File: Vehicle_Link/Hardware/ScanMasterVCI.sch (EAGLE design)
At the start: 97 parts, among them IC1 XMEGA32A4U, IC2 TL331, Q1 MMBT4403, Q10 ZXMP6A17G, Q2 MMBT3904, Q3 MMBT3904, Q4 MMBT4403, Q7 MMBT3904, Q8 MMBT4403, Q9 MMPQ3904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

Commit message: CCD RX circuit tested. Don't have the firmware in a state to test the TX but I want to move forward with new boards for testing. I've finished re-laying out the board. Made a minor change to J1850, switched to a comparator for the RX.
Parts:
- added IC3: TL331, linear:TL331
- added R41: 10k, adafruit:R-US_R0603
- R2: value 7.5k -> 1k
- R3: value 5k -> 1k
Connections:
- removed net SCI-A-ENGINE-EN: IC1.PB0
- removed net SCI-A-TRANS-EN: IC1.PB2
- removed net SCI-B-ENGINE-EN: IC1.PB1
- removed net SCI-B-TRANS-EN: IC1.PB3
- new net N$37: IC3.+IN, R2.1, R3.2
- net +3V3: now also IC3.V+, R41.2
- net +8V: now also R2.2
- net CCD-RX: now also R41.1
- net GND: now also IC3.GND
- net J1850VPW-RX: now also IC3.OUT; no longer R2.1, R3.2
- net J1962-2: now also IC3.-IN; no longer R2.2
- net SCI-A-EN: now also IC1.PB0
- net SCI-B-EN: now also IC1.PB1
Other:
- moved on the sheet: R2, R3

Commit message: Worked on the board layout some more - tried to trim down on some vias.
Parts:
- removed C3: 0.1uF, adafruit:C-USC0603
- removed R41: 10k, adafruit:R-US_R0603
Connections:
- net +3V3: no longer C3.1, R41.2
- net CCD-RX: no longer R41.1
- net GND: no longer C3.2
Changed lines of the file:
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@@
 <grid distance="0.1" unitdist="inch" unit="inch" style="lines" multiple="1" display="no" altdistance="0.01" altunitdist="inch" altunit="inch"/>
 <layers>
-<layer number="1" name="Top" color="4" fill="1" visible="yes" active="no"/>
-<layer number="16" name="Bottom" color="1" fill="1" visible="yes" active="no"/>
-<layer number="17" name="Pads" color="2" fill="1" visible="yes" active="no"/>
-<layer number="18" name="Vias" color="2" fill="1" visible="yes" active="no"/>
-<layer number="19" name="Unrouted" color="6" fill="1" visible="yes" active="no"/>
-<layer number="20" name="Dimension" color="24" fill="1" visible="yes" active="no"/>
-<layer number="21" name="tPlace" color="7" fill="1" visible="yes" active="no"/>
-<layer number="22" name="bPlace" color="7" fill="1" visible="yes" active="no"/>
-<layer number="23" name="tOrigins" color="15" fill="1" visible="yes" active="no"/>
-<layer number="24" name="bOrigins" color="15" fill="1" visible="yes" active="no"/>
-<layer number="25" name="tNames" color="7" fill="1" visible="yes" active="no"/>
-<layer number="26" name="bNames" color="7" fill="1" visible="yes" active="no"/>
-<layer number="27" name="tValues" color="7" fill="1" visible="yes" active="no"/>
-<layer number="28" name="bValues" color="7" fill="1" visible="yes" active="no"/>
+<layer number="1" name="Top" color="4" fill="1" visible="no" active="no"/>
+<layer number="16" name="Bottom" color="1" fill="1" visible="no" active="no"/>
+<layer number="17" name="Pads" color="2" fill="1" visible="no" active="no"/>
+<layer number="18" name="Vias" color="2" fill="1" visible="no" active="no"/>
+<layer number="19" name="Unrouted" color="6" fill="1" visible="no" active="no"/>
+<layer number="20" name="Dimension" color="24" fill="1" visible="no" active="no"/>
+<layer number="21" name="tPlace" color="7" fill="1" visible="no" active="no"/>
+<layer number="22" name="bPlace" color="7" fill="1" visible="no" active="no"/>
+<layer number="23" name="tOrigins" color="15" fill="1" visible="no" active="no"/>
+<layer number="24" name="bOrigins" color="15" fill="1" visible="no" active="no"/>
+<layer number="25" name="tNames" color="7" fill="1" visible="no" active="no"/>
+<layer number="26" name="bNames" color="7" fill="1" visible="no" active="no"/>
+<layer number="27" name="tValues" color="7" fill="1" visible="no" active="no"/>
+<layer number="28" name="bValues" color="7" fill="1" visible="no" active="no"/>
 <layer number="29" name="tStop" color="7" fill="3" visible="no" active="no"/>
 <layer number="30" name="bStop" color="7" fill="6" visible="no" active="no"/>
@@
 <layer number="35" name="tGlue" color="7" fill="4" visible="no" active="no"/>
 <layer number="36" name="bGlue" color="7" fill="5" visible="no" active="no"/>
-<layer number="37" name="tTest" color="7" fill="1" visible="yes" active="no"/>
-<layer number="38" name="bTest" color="7" fill="1" visible="yes" active="no"/>
+<layer number="37" name="tTest" color="7" fill="1" visible="no" active="no"/>
+<layer number="38" name="bTest" color="7" fill="1" visible="no" active="no"/>
 <layer number="39" name="tKeepout" color="4" fill="11" visible="no" active="no"/>
 <layer number="40" name="bKeepout" color="1" fill="11" visible="no" active="no"/>
@@
 <layer number="44" name="Drills" color="7" fill="1" visible="no" active="no"/>
 <layer number="45" name="Holes" color="7" fill="1" visible="no" active="no"/>
-<layer number="46" name="Milling" color="3" fill="1" visible="yes" active="no"/>
-<layer number="47" name="Measures" color="7" fill="1" visible="yes" active="no"/>
-<layer number="48" name="Document" color="7" fill="1" visible="yes" active="no"/>
-<layer number="49" name="Reference" color="7" fill="1" visible="yes" active="no"/>
-<layer number="50" name="dxf" color="7" fill="1" visible="yes" active="no"/>
-<layer number="51" name="tDocu" color="7" fill="1" visible="yes" active="no"/>
-<layer number="52" name="bDocu" color="7" fill="1" visible="yes" active="no"/>
-<layer number="53" name="tGND_GNDA" color="7" fill="9" visible="yes" active="no"/>
-<layer number="54" name="bGND_GNDA" color="1" fill="9" visible="yes" active="no"/>
-<layer number="56" name="wert" color="7" fill="1" visible="yes" active="no"/>
-<layer number="57" name="tCAD" color="7" fill="1" visible="yes" active="no"/>
-<layer number="59" name="tCarbon" color="7" fill="1" visible="yes" active="no"/>
-<layer number="60" name="bCarbon" color="7" fill="1" visible="yes" active="no"/>
-<layer number="61" name="stand" color="7" fill="1" visible="yes" active="no"/>
+<layer number="46" name="Milling" color="3" fill="1" visible="no" active="no"/>
+<layer number="47" name="Measures" color="7" fill="1" visible="no" active="no"/>
+<layer number="48" name="Document" color="7" fill="1" visible="no" active="no"/>
+<layer number="49" name="Reference" color="7" fill="1" visible="no" active="no"/>
+<layer number="50" name="dxf" color="7" fill="1" visible="no" active="no"/>
+<layer number="51" name="tDocu" color="7" fill="1" visible="no" active="no"/>
+<layer number="52" name="bDocu" color="7" fill="1" visible="no" active="no"/>
+<layer number="53" name="tGND_GNDA" color="7" fill="9" visible="no" active="no"/>
+<layer number="54" name="bGND_GNDA" color="1" fill="9" visible="no" active="no"/>
+<layer number="56" name="wert" color="7" fill="1" visible="no" active="no"/>
+<layer number="57" name="tCAD" color="7" fill="1" visible="no" active="no"/>
+<layer number="59" name="tCarbon" color="7" fill="1" visible="no" active="no"/>
+<layer number="60" name="bCarbon" color="7" fill="1" visible="no" active="no"/>
+<layer number="61" name="stand" color="7" fill="1" visible="no" active="no"/>
 <layer number="88" name="SimResults" color="9" fill="1" visible="yes" active="yes"/>
 <layer number="89" name="SimProbes" color="9" fill="1" visible="yes" active="yes"/>
@@
 <part name="RN3" library="resistor-net" library_urn="urn:adsk.eagle:library:343" deviceset="CTS742C083" device="" package3d_urn="urn:adsk.eagle:package:24985/1" value="100k"/>
 <part name="+3V6" library="supply1" library_urn="urn:adsk.eagle:library:371" deviceset="+3V3" device=""/>
-<part name="C3" library="adafruit" library_urn="urn:adsk.eagle:library:420" deviceset="C-US" device="C0603" value="0.1uF"/>
-<part name="GND42" library="supply1" library_urn="urn:adsk.eagle:library:371" deviceset="GND" device=""/>
 <part name="LED1" library="led" library_urn="urn:adsk.eagle:library:259" deviceset="LED" device="CHIP-LED0603" package3d_urn="urn:adsk.eagle:package:15819/1" value="RED"/>
 <part name="R24" library="resistor" library_urn="urn:adsk.eagle:library:348" deviceset="R-US_" device="R0603" package3d_urn="urn:adsk.eagle:package:26057/1" value="120"/>
@@
 <part name="GND37" library="supply1" library_urn="urn:adsk.eagle:library:371" deviceset="GND" device=""/>
 <part name="GND45" library="supply1" library_urn="urn:adsk.eagle:library:371" deviceset="GND" device=""/>
-<part name="R41" library="adafruit" library_urn="urn:adsk.eagle:library:420" deviceset="R-US_" device="R0603" value="10k"/>
-<part name="+3V9" library="supply1" library_urn="urn:adsk.eagle:library:371" deviceset="+3V3" device=""/>
 </parts>
 <sheets>
@@
 <instance part="RN3" gate="G$1" x="193.04" y="71.12"/>
 <instance part="+3V6" gate="G$1" x="215.9" y="83.82"/>
-<instance part="C3" gate="G$1" x="226.06" y="68.58" rot="MR0"/>
-<instance part="GND42" gate="1" x="226.06" y="58.42"/>
 <instance part="U2" gate="G$1" x="45.72" y="195.58" rot="MR0"/>
 <instance part="GND3" gate="1" x="60.96" y="182.88"/>
@@
 <instance part="GND37" gate="1" x="154.94" y="154.94"/>
 <instance part="GND45" gate="1" x="154.94" y="152.4"/>
-<instance part="R41" gate="G$1" x="104.14" y="238.76" smashed="yes" rot="R90">
-<attribute name="NAME" x="102.87" y="242.3414" size="1.778" layer="95" rot="R180"/>
-<attribute name="VALUE" x="102.87" y="236.982" size="1.778" layer="96" rot="R180"/>
-</instance>
-<instance part="+3V9" gate="G$1" x="104.14" y="248.92"/>
 </instances>
 <busses>
@@
 <pinref part="+3V6" gate="G$1" pin="+3V3"/>
 <wire x1="215.9" y1="71.12" x2="215.9" y2="73.66" width="0.1524" layer="91"/>
-<wire x1="215.9" y1="73.66" x2="215.9" y2="78.74" width="0.1524" layer="91"/>
-<wire x1="215.9" y1="78.74" x2="215.9" y2="81.28" width="0.1524" layer="91"/>
-<wire x1="215.9" y1="78.74" x2="226.06" y2="78.74" width="0.1524" layer="91"/>
-<junction x="215.9" y="78.74"/>
-<wire x1="226.06" y1="78.74" x2="226.06" y2="71.12" width="0.1524" layer="91"/>
-<pinref part="C3" gate="G$1" pin="1"/>
+<wire x1="215.9" y1="73.66" x2="215.9" y2="81.28" width="0.1524" layer="91"/>
 <pinref part="RN3" gate="G$1" pin="7"/>
 <wire x1="200.66" y1="71.12" x2="215.9" y2="71.12" width="0.1524" layer="91"/>
@@
 <pinref part="IC3" gate="G$1" pin="V+"/>
 <wire x1="170.18" y1="182.88" x2="170.18" y2="177.8" width="0.1524" layer="91"/>
-</segment>
-<segment>
-<pinref part="R41" gate="G$1" pin="2"/>
-<pinref part="+3V9" gate="G$1" pin="+3V3"/>
-<wire x1="104.14" y1="246.38" x2="104.14" y2="243.84" width="0.1524" layer="91"/>
 </segment>
 </net>
@@
 </segment>
 <segment>
-<pinref part="C3" gate="G$1" pin="2"/>
-<pinref part="GND42" gate="1" pin="GND"/>
-<wire x1="226.06" y1="60.96" x2="226.06" y2="63.5" width="0.1524" layer="91"/>
-</segment>
-<segment>
 <pinref part="U2" gate="G$1" pin="DI"/>
 <wire x1="60.96" y1="193.04" x2="60.96" y2="185.42" width="0.1524" layer="91"/>
@@
 <wire x1="68.58" y1="233.68" x2="88.9" y2="233.68" width="0.1524" layer="91"/>
 <wire x1="88.9" y1="233.68" x2="88.9" y2="243.84" width="0.1524" layer="91"/>
-<wire x1="88.9" y1="233.68" x2="104.14" y2="233.68" width="0.1524" layer="91"/>
+<wire x1="88.9" y1="233.68" x2="111.76" y2="233.68" width="0.1524" layer="91"/>
 <junction x="88.9" y="233.68"/>
 <label x="111.76" y="233.68" size="1.27" layer="95" xref="yes"/>
-<pinref part="R41" gate="G$1" pin="1"/>
-<wire x1="104.14" y1="233.68" x2="111.76" y2="233.68" width="0.1524" layer="91"/>
-<junction x="104.14" y="233.68"/>
-</segment>
-<segment>
+</segment>
+<segment>

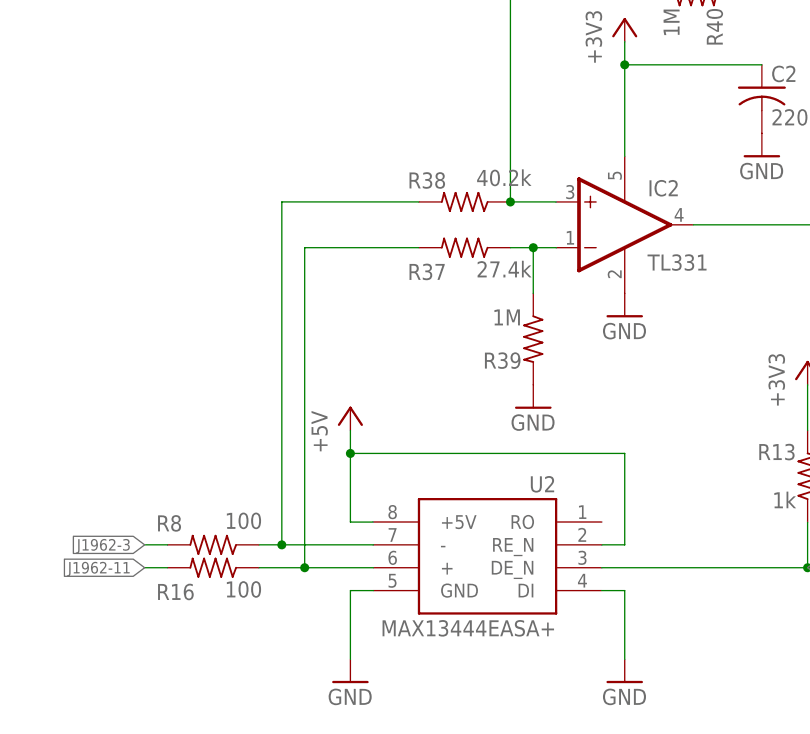
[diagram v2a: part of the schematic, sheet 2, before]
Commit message: Reviewed the CCD circuit and found some small issues with the RX circuit, fixed.
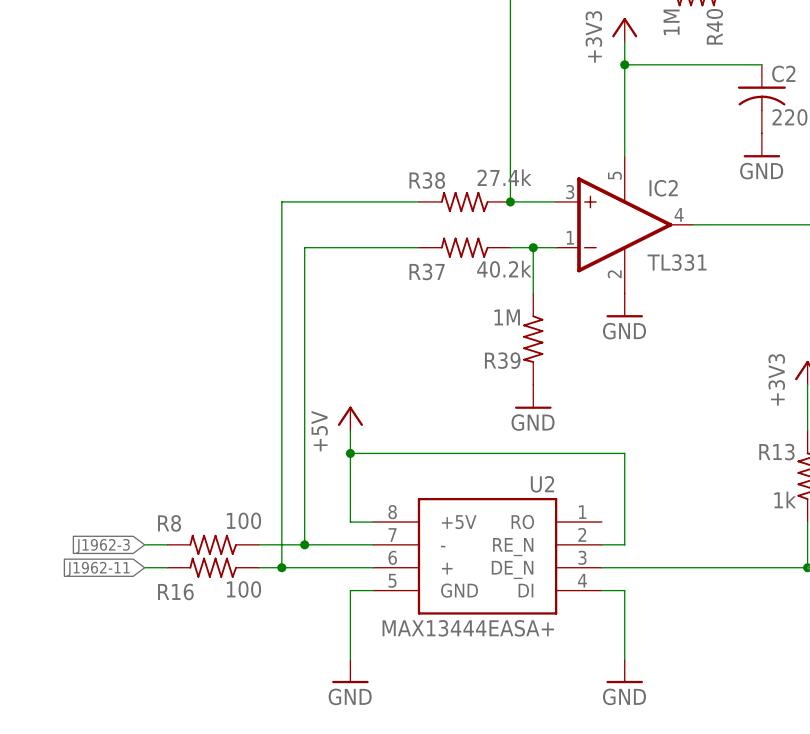
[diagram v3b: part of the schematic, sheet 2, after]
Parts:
- R37: value 27.4k -> 40.2k
- R38: value 40.2k -> 27.4k
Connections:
- removed net N$32: R16.1, R37.2, U2.+
- new net N$39: R37.2, R8.1, U2.-
- net N$33: now also R16.1, U2.+; no longer R8.1, U2.-
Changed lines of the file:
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@@
 <?xml version="1.0" encoding="utf-8"?>
 <!DOCTYPE eagle SYSTEM "eagle.dtd">
-<eagle version="8.7.0">
+<eagle version="8.4.3">
 <drawing>
 <settings>
@@
 <part name="R8" library="adafruit" library_urn="urn:adsk.eagle:library:420" deviceset="R-US_" device="R0603" value="100"/>
 <part name="R16" library="adafruit" library_urn="urn:adsk.eagle:library:420" deviceset="R-US_" device="R0603" value="100"/>
-<part name="R37" library="adafruit" library_urn="urn:adsk.eagle:library:420" deviceset="R-US_" device="R0603" value="27.4k"/>
-<part name="R38" library="adafruit" library_urn="urn:adsk.eagle:library:420" deviceset="R-US_" device="R0603" value="40.2k"/>
+<part name="R37" library="adafruit" library_urn="urn:adsk.eagle:library:420" deviceset="R-US_" device="R0603" value="40.2k"/>
+<part name="R38" library="adafruit" library_urn="urn:adsk.eagle:library:420" deviceset="R-US_" device="R0603" value="27.4k"/>
 <part name="IC2" library="linear" library_urn="urn:adsk.eagle:library:262" deviceset="TL331" device="" package3d_urn="urn:adsk.eagle:package:16494/1"/>
 <part name="R39" library="adafruit" library_urn="urn:adsk.eagle:library:420" deviceset="R-US_" device="R0603" value="1M"/>
@@
 </segment>
 </net>
-<net name="N$32" class="0">
-<segment>
+<net name="N$33" class="0">
+<segment>
+<wire x1="22.86" y1="236.22" x2="38.1" y2="236.22" width="0.1524" layer="91"/>
+<pinref part="R38" gate="G$1" pin="2"/>
 <pinref part="R16" gate="G$1" pin="1"/>
 <pinref part="U2" gate="G$1" pin="+"/>
-<wire x1="20.32" y1="195.58" x2="25.4" y2="195.58" width="0.1524" layer="91"/>
-<wire x1="25.4" y1="195.58" x2="33.02" y2="195.58" width="0.1524" layer="91"/>
-<wire x1="25.4" y1="195.58" x2="25.4" y2="231.14" width="0.1524" layer="91"/>
-<junction x="25.4" y="195.58"/>
-<wire x1="25.4" y1="231.14" x2="38.1" y2="231.14" width="0.1524" layer="91"/>
-<pinref part="R37" gate="G$1" pin="2"/>
-</segment>
-</net>
-<net name="N$33" class="0">
-<segment>
-<pinref part="R8" gate="G$1" pin="1"/>
-<pinref part="U2" gate="G$1" pin="-"/>
-<wire x1="20.32" y1="198.12" x2="22.86" y2="198.12" width="0.1524" layer="91"/>
-<wire x1="22.86" y1="198.12" x2="33.02" y2="198.12" width="0.1524" layer="91"/>
-<wire x1="22.86" y1="198.12" x2="22.86" y2="236.22" width="0.1524" layer="91"/>
-<wire x1="22.86" y1="236.22" x2="38.1" y2="236.22" width="0.1524" layer="91"/>
-<junction x="22.86" y="198.12"/>
-<pinref part="R38" gate="G$1" pin="2"/>
+<wire x1="20.32" y1="195.58" x2="22.86" y2="195.58" width="0.1524" layer="91"/>
+<wire x1="22.86" y1="195.58" x2="33.02" y2="195.58" width="0.1524" layer="91"/>
+<wire x1="22.86" y1="236.22" x2="22.86" y2="195.58" width="0.1524" layer="91"/>
+<junction x="22.86" y="195.58"/>
 </segment>
 </net>
@@
 </segment>
 </net>
+<net name="N$39" class="0">
+<segment>
+<pinref part="U2" gate="G$1" pin="-"/>
+<pinref part="R8" gate="G$1" pin="1"/>
+<wire x1="20.32" y1="198.12" x2="25.4" y2="198.12" width="0.1524" layer="91"/>
+<pinref part="R37" gate="G$1" pin="2"/>
+<wire x1="25.4" y1="198.12" x2="33.02" y2="198.12" width="0.1524" layer="91"/>
+<wire x1="25.4" y1="231.14" x2="38.1" y2="231.14" width="0.1524" layer="91"/>
+<wire x1="25.4" y1="198.12" x2="25.4" y2="231.14" width="0.1524" layer="91"/>
+<junction x="25.4" y="198.12"/>
+</segment>
+</net>
